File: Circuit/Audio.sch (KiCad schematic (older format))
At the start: 10 parts, among them U5 NAU8814

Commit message: Speaker choice changed & footprint creation.
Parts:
- MK1: footprint (none) -> libs1:MEMSMicrophone-SMT-SPU0410HR5H‐PB
- SP1: footprint (none) -> libs1:CVS-1508.Speaker.PCPins; Digikey PN 102-2494-ND -> 102-2498-ND; Link http://www.digikey.com.au/product-detail/en/cui-inc/CDM-120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 -> http://www.digikey.com.au/product-detail/en/cui-inc/CVS-150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; Manufacturer PN CDM-12008 -> CVS-1508; Unit Cost 2.44000 -> 3.3600
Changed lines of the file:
@@
 F 0 "SP1" H 7400 3150 50  0000 C CNN
 F 1 "SPEAKER" H 7400 2650 50  0000 C CNN
-F 2 "" H 7500 2900 50  0001 C CNN
+F 2 "libs1:CVS-1508.Speaker.PCPins" H 7500 2900 50  0001 C CNN
 F 3 "" H 7500 2900 50  0000 C CNN
-F 4 "http://www.digikey.com.au/product-detail/en/cui-inc/CDM-12008/102-2494-ND/2791824" H 7500 2900 60  0001 C CNN "Link"
-F 5 "2.44000" H 7500 2900 60  0001 C CNN "Unit Cost"
-F 6 "102-2494-ND" H 7500 2900 60  0001 C CNN "Digikey PN"
-F 7 "CDM-12008" H 7500 2900 60  0001 C CNN "Manufacturer PN"
+F 4 "http://www.digikey.com.au/product-detail/en/cui-inc/CVS-1508/102-2498-ND/2791828" H 7500 2900 60  0001 C CNN "Link"
+F 5 "3.3600" H 7500 2900 60  0001 C CNN "Unit Cost"
+F 6 "102-2498-ND" H 7500 2900 60  0001 C CNN "Digikey PN"
+F 7 "CVS-1508" H 7500 2900 60  0001 C CNN "Manufacturer PN"
 	1    7500 2900
 	1    0    0    -1
@@
 F 0 "MK1" H 1200 2200 60  0000 C CNN
 F 1 "SPU0410HR5H" H 900 1550 60  0000 C CNN
-F 2 "" H 1400 1900 60  0001 C CNN
+F 2 "libs1:MEMSMicrophone-SMT-SPU0410HR5H‐PB" H 1400 1900 60  0001 C CNN
 F 3 "" H 1400 1900 60  0001 C CNN
 	1    1400 1900

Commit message: Begin adding fields to components.
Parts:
- U5: Digikey PN (none) -> NAU8814YG-ND; Link (none) -> http://www.digikey.com.au/product-detail/en/nuvoton-technol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; Manufacturer PN (none) -> NAU8814YG; Unit Price (none) -> 3.06
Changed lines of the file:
@@
 F 2 "" H 5600 3750 60  0001 C CNN
 F 3 "" H 5600 3750 60  0001 C CNN
+F 4 "NAU8814YG-ND" H 5600 3750 60  0001 C CNN "Digikey PN"
+F 5 "http://www.digikey.com.au/product-detail/en/nuvoton-technology-corporation-of-america/NAU8814YG/NAU8814YG-ND/4271437" H 5600 3750 60  0001 C CNN "Link"
+F 6 "NAU8814YG" H 5600 3750 60  0001 C CNN "Manufacturer PN"
+F 7 "3.06" H 5600 3750 60  0001 C CNN "Unit Price"
 	1    5600 3750
 	1    0    0    -1

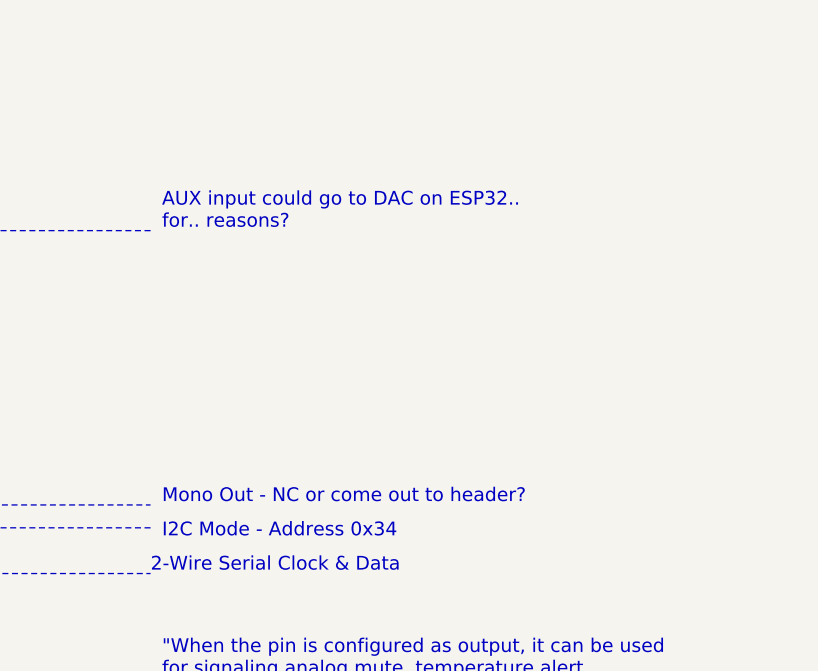
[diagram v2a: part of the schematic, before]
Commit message: IR receiver schematic & footprint.
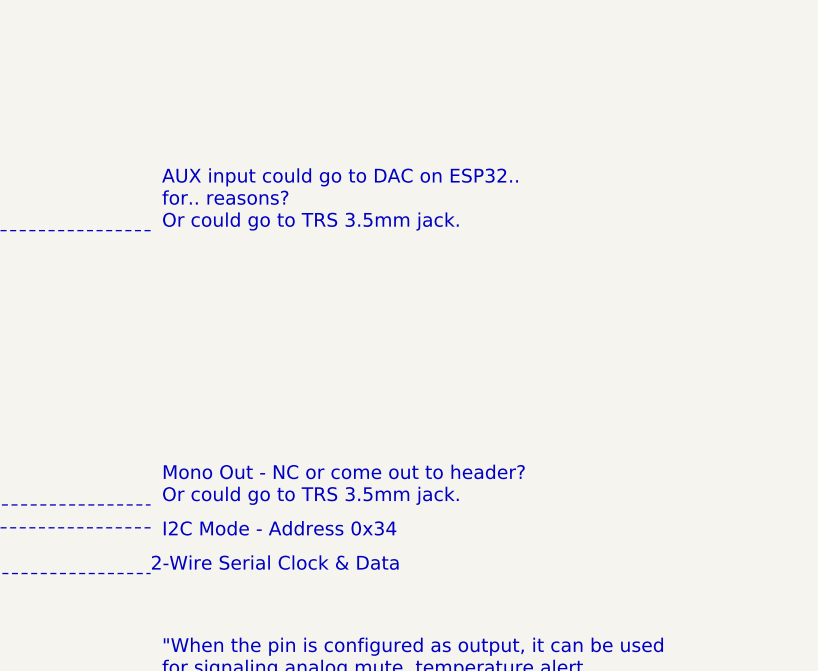
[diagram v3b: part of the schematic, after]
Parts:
- C1, C13, C14, C15, C16: footprint (none) -> Capacitors_SMD:C_0603_HandSoldering; Digikey PN (none) -> 1276-2087-1-ND; Link (none) -> http://www.digikey.com.au/product-detail/en/samsung-electro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; Manufacturer PN (none) -> CL10B475KQ8NQNC; Unit Cost (none) -> 0.01
- MK1: footprint libs1:MEMSMicrophone-SMT-SPU0410HR5H‐PB -> libs:MEMSMicrophone-SMT-SPU0410HR5H‐PB
- SP1: footprint libs1:CVS-1508.Speaker.PCPins -> libs:CVS-1508.Speaker.PCPins
- U5: footprint (none) -> libs:NAU8814_QFN-24_4x4mm_Pitch0.5mm_EPAD
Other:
- note added: "AUX input could go to DAC on ESP32..\nfor.. reasons?\nOr could go to TRS 3.5mm jack."
- note added: "Mono Out - NC or come out to header?\nOr could go to TRS 3.5mm jack."
- note removed: "AUX input could go to DAC on ESP32..\nfor.. reasons?"
- note removed: "Mono Out - NC or come out to header?"
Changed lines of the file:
@@
 F 0 "U5" H 5000 4450 60  0000 C CNN
 F 1 "NAU8814" H 6150 3050 60  0000 C CNN
-F 2 "" H 5600 3750 60  0001 C CNN
+F 2 "libs:NAU8814_QFN-24_4x4mm_Pitch0.5mm_EPAD" H 5600 3750 60  0001 C CNN
 F 3 "" H 5600 3750 60  0001 C CNN
 F 4 "NAU8814YG-ND" H 5600 3750 60  0001 C CNN "Digikey PN"
@@
 F 0 "SP1" H 7400 3150 50  0000 C CNN
 F 1 "SPEAKER" H 7400 2650 50  0000 C CNN
-F 2 "libs1:CVS-1508.Speaker.PCPins" H 7500 2900 50  0001 C CNN
+F 2 "libs:CVS-1508.Speaker.PCPins" H 7500 2900 50  0001 C CNN
 F 3 "" H 7500 2900 50  0000 C CNN
 F 4 "http://www.digikey.com.au/product-detail/en/cui-inc/CVS-1508/102-2498-ND/2791828" H 7500 2900 60  0001 C CNN "Link"
@@
 F 0 "MK1" H 1200 2200 60  0000 C CNN
 F 1 "SPU0410HR5H" H 900 1550 60  0000 C CNN
-F 2 "libs1:MEMSMicrophone-SMT-SPU0410HR5H‐PB" H 1400 1900 60  0001 C CNN
+F 2 "libs:MEMSMicrophone-SMT-SPU0410HR5H‐PB" H 1400 1900 60  0001 C CNN
 F 3 "" H 1400 1900 60  0001 C CNN
 	1    1400 1900
@@
 F 0 "C16" H 5575 2400 50  0000 L CNN
 F 1 "4.7uF" H 5575 2200 50  0000 L CNN
-F 2 "" H 5588 2150 50  0001 C CNN
+F 2 "Capacitors_SMD:C_0603_HandSoldering" H 5588 2150 50  0001 C CNN
 F 3 "" H 5550 2300 50  0000 C CNN
+F 4 "1276-2087-1-ND" H 3600 4150 60  0001 C CNN "Digikey PN"
+F 5 "http://www.digikey.com.au/product-detail/en/samsung-electro-mechanics-america-inc/CL10B475KQ8NQNC/1276-2087-1-ND/3890173" H 3600 4150 60  0001 C CNN "Link"
+F 6 "CL10B475KQ8NQNC" H 3600 4150 60  0001 C CNN "Manufacturer PN"
+F 7 "0.01" H 3600 4150 60  0001 C CNN "Unit Cost"
 	1    5550 2300
 	1    0    0    -1
@@
 F 0 "C13" H 3625 4250 50  0000 L CNN
 F 1 "4.7uF" H 3625 4050 50  0000 L CNN
-F 2 "" H 3638 4000 50  0001 C CNN
+F 2 "Capacitors_SMD:C_0603_HandSoldering" H 3638 4000 50  0001 C CNN
 F 3 "" H 3600 4150 50  0000 C CNN
+F 4 "1276-2087-1-ND" H 3600 4150 60  0001 C CNN "Digikey PN"
+F 5 "http://www.digikey.com.au/product-detail/en/samsung-electro-mechanics-america-inc/CL10B475KQ8NQNC/1276-2087-1-ND/3890173" H 3600 4150 60  0001 C CNN "Link"
+F 6 "CL10B475KQ8NQNC" H 3600 4150 60  0001 C CNN "Manufacturer PN"
+F 7 "0.01" H 3600 4150 60  0001 C CNN "Unit Cost"
 	1    3600 4150
 	1    0    0    -1
@@
 F 0 "C14" H 3875 4250 50  0000 L CNN
 F 1 "4.7uF" H 3875 4050 50  0000 L CNN
-F 2 "" H 3888 4000 50  0001 C CNN
+F 2 "Capacitors_SMD:C_0603_HandSoldering" H 3888 4000 50  0001 C CNN
 F 3 "" H 3850 4150 50  0000 C CNN
+F 4 "1276-2087-1-ND" H 3600 4150 60  0001 C CNN "Digikey PN"
+F 5 "http://www.digikey.com.au/product-detail/en/samsung-electro-mechanics-america-inc/CL10B475KQ8NQNC/1276-2087-1-ND/3890173" H 3600 4150 60  0001 C CNN "Link"
+F 6 "CL10B475KQ8NQNC" H 3600 4150 60  0001 C CNN "Manufacturer PN"
+F 7 "0.01" H 3600 4150 60  0001 C CNN "Unit Cost"
 	1    3850 4150
 	1    0    0    -1
@@
 F 0 "C15" H 4125 4250 50  0000 L CNN
 F 1 "4.7uF" H 4125 4050 50  0000 L CNN
-F 2 "" H 4138 4000 50  0001 C CNN
+F 2 "Capacitors_SMD:C_0603_HandSoldering" H 4138 4000 50  0001 C CNN
 F 3 "" H 4100 4150 50  0000 C CNN
+F 4 "1276-2087-1-ND" H 3600 4150 60  0001 C CNN "Digikey PN"
+F 5 "http://www.digikey.com.au/product-detail/en/samsung-electro-mechanics-america-inc/CL10B475KQ8NQNC/1276-2087-1-ND/3890173" H 3600 4150 60  0001 C CNN "Link"
+F 6 "CL10B475KQ8NQNC" H 3600 4150 60  0001 C CNN "Manufacturer PN"
+F 7 "0.01" H 3600 4150 60  0001 C CNN "Unit Cost"
 	1    4100 4150
 	1    0    0    -1
@@
 F 0 "C1" H 825 2000 50  0000 L CNN
 F 1 "4.7uF" H 825 1800 50  0000 L CNN
-F 2 "" H 838 1750 50  0001 C CNN
+F 2 "Capacitors_SMD:C_0603_HandSoldering" H 838 1750 50  0001 C CNN
 F 3 "" H 800 1900 50  0000 C CNN
+F 4 "1276-2087-1-ND" H 3600 4150 60  0001 C CNN "Digikey PN"
+F 5 "http://www.digikey.com.au/product-detail/en/samsung-electro-mechanics-america-inc/CL10B475KQ8NQNC/1276-2087-1-ND/3890173" H 3600 4150 60  0001 C CNN "Link"
+F 6 "CL10B475KQ8NQNC" H 3600 4150 60  0001 C CNN "Manufacturer PN"
+F 7 "0.01" H 3600 4150 60  0001 C CNN "Unit Cost"
 	1    800  1900
 	1    0    0    -1
@@
 	6800 3700 9550 3700
 Text Notes 9600 3700 0    60   ~ 0
-Mono Out - NC or come out to header?
+Mono Out - NC or come out to header?\nOr could go to TRS 3.5mm jack.
 $Comp
 L GND #PWR063
@@
 	5650 2500 5650 2800
 Text Notes 9600 2500 0    60   ~ 0
-AUX input could go to DAC on ESP32..\nfor.. reasons?
+AUX input could go to DAC on ESP32..\nfor.. reasons?\nOr could go to TRS 3.5mm jack.
 $Comp
 L GND #PWR066

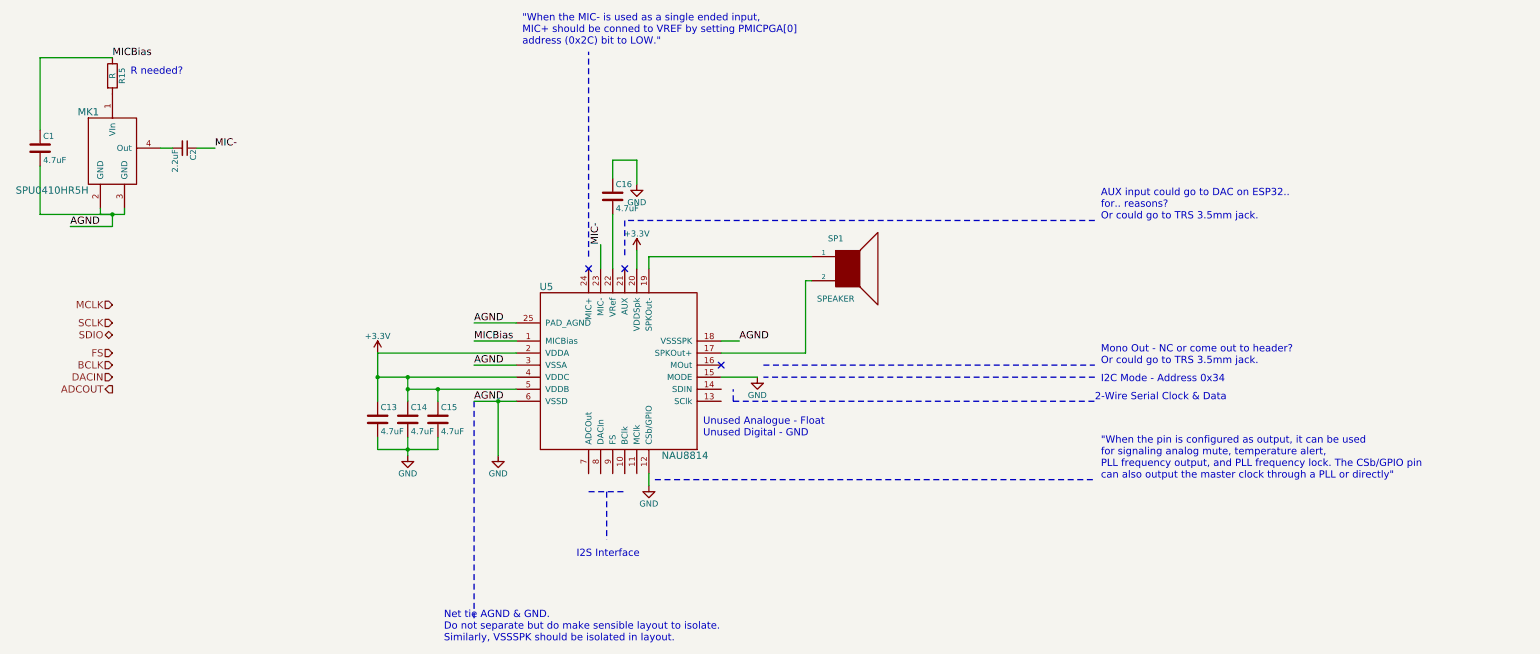
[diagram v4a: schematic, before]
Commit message: Adding some component information, connecting audio.
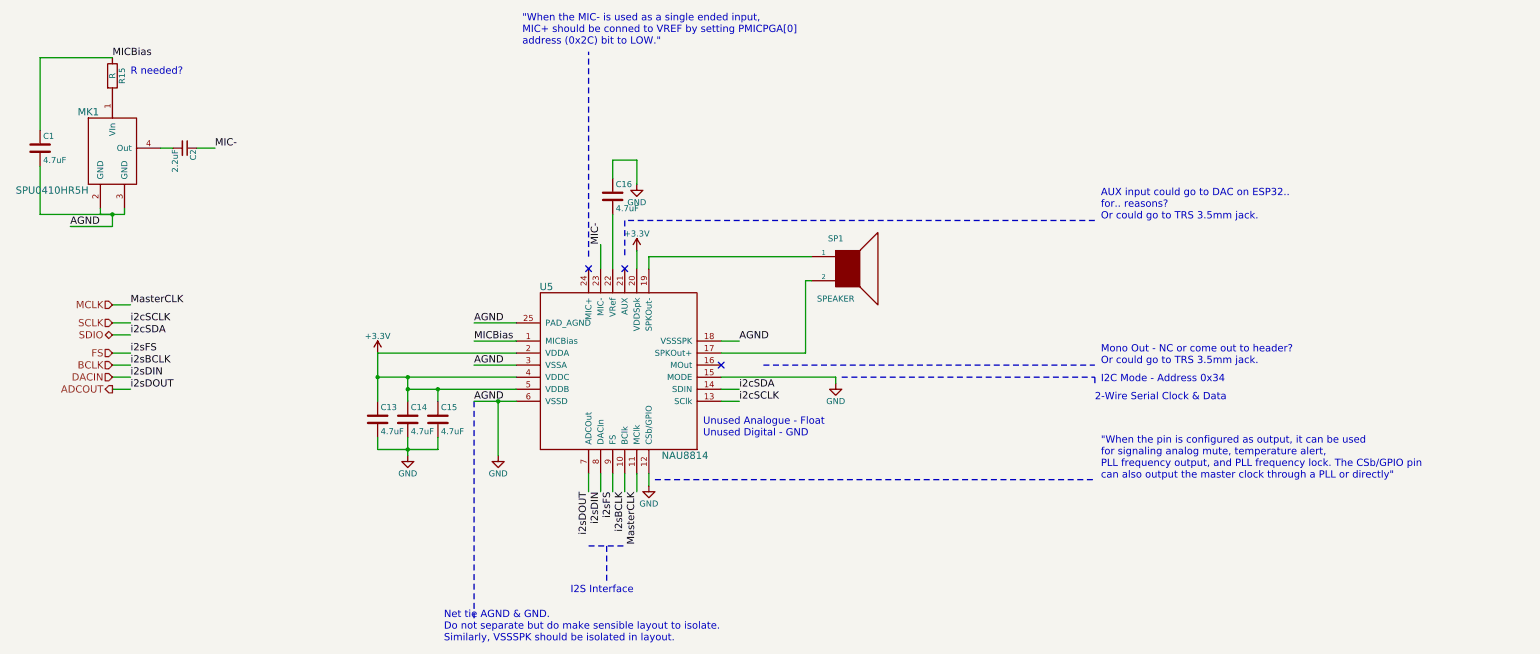
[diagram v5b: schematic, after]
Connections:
- net ADCOUT: now also U5.7 (ADCOut)
- net BCLK: now also U5.10 (BClk)
- net DACIN: now also U5.8 (DACIn)
- net FS: now also U5.9 (FS)
- net MCLK: now also U5.11 (MClk)
- net SCLK: now also U5.13 (SClk)
- net SDIO: now also U5.14 (SDIN)
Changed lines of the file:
@@
 L GND #PWR061
 U 1 1 581BF41C
-P 6750 3800
-F 0 "#PWR061" H 6750 3550 50  0001 C CNN
-F 1 "GND" H 6750 3650 50  0000 C CNN
-F 2 "" H 6750 3800 50  0000 C CNN
-F 3 "" H 6750 3800 50  0000 C CNN
-	1    6750 3800
-	1    0    0    -1
-$EndComp
-Wire Wire Line
-	6450 3800 6750 3800
+P 7400 3850
+F 0 "#PWR061" H 7400 3600 50  0001 C CNN
+F 1 "GND" H 7400 3700 50  0000 C CNN
+F 2 "" H 7400 3850 50  0000 C CNN
+F 3 "" H 7400 3850 50  0000 C CNN
+	1    7400 3850
+	1    0    0    -1
+$EndComp
+Wire Wire Line
+	6450 3800 7400 3800
 Text Notes 9600 3850 0    60   ~ 0
 I2C Mode - Address 0x34
@@
 Wire Wire Line
 	7150 3600 6450 3600
-Wire Notes Line
-	9550 3800 6800 3800
 Wire Notes Line
 	6800 3700 9550 3700
@@
 "When the pin is configured as output, it can be used\nfor signaling analog mute, temperature alert, \nPLL frequency output, and PLL frequency lock. The CSb/GPIO pin\ncan also output the master clock through a PLL or directly"
 NoConn ~ 6450 3700
-Wire Notes Line
-	6550 4000 9550 4000
 Text Notes 9550 4000 0    60   ~ 0
  2-Wire Serial Clock & Data
 Wire Notes Line
-	6550 4000 6550 3900
-Wire Notes Line
-	5350 4750 5650 4750
-Wire Notes Line
-	5500 4750 5500 5150
-Text Notes 5250 5300 0    60   ~ 0
-I2S Interface
+	5350 5200 5650 5200
 Text HLabel 1400 3200 0    60   Input ~ 0
 MCLK
@@
 Text HLabel 1400 3900 0    60   Output ~ 0
 ADCOUT
+Text Label 1550 3350 0    60   ~ 0
+i2cSCLK
+Text Label 1550 3450 0    60   ~ 0
+i2cSDA
+Text Label 1550 3600 0    60   ~ 0
+i2sFS
+Text Label 1550 3700 0    60   ~ 0
+i2sBCLK
+Text Label 1550 3800 0    60   ~ 0
+i2sDIN
+Text Label 1550 3900 0    60   ~ 0
+i2sDOUT
+Text Label 1550 3200 0    60   ~ 0
+MasterCLK
+Text Label 5750 4750 3    60   ~ 0
+MasterCLK
+Text Label 5550 4750 3    60   ~ 0
+i2sFS
+Text Label 5650 4750 3    60   ~ 0
+i2sBCLK
+Text Label 5450 4750 3    60   ~ 0
+i2sDIN
+Text Label 5350 4750 3    60   ~ 0
+i2sDOUT
+Text Notes 5200 5600 0    60   ~ 0
+I2S Interface
+Wire Notes Line
+	5500 5200 5500 5500
+Wire Wire Line
+	5350 4600 5350 4750
+Wire Wire Line
+	5450 4600 5450 4750
+Wire Wire Line
+	5550 4600 5550 4750
+Wire Wire Line
+	5650 4600 5650 4750
+Wire Wire Line
+	5750 4600 5750 4750
+Text Label 6600 4000 0    60   ~ 0
+i2cSCLK
+Text Label 6600 3900 0    60   ~ 0
+i2cSDA
+Wire Wire Line
+	7400 3800 7400 3850
+Wire Notes Line
+	7450 3800 9550 3800
+Wire Notes Line
+	9550 3800 9550 3850
+Wire Wire Line
+	6450 3900 6600 3900
+Wire Wire Line
+	6450 4000 6600 4000
+Wire Wire Line
+	1400 3200 1550 3200
+Wire Wire Line
+	1400 3350 1550 3350
+Wire Wire Line
+	1400 3450 1550 3450
+Wire Wire Line
+	1400 3600 1550 3600
+Wire Wire Line
+	1400 3700 1550 3700
+Wire Wire Line
+	1400 3800 1550 3800
+Wire Wire Line
+	1400 3900 1550 3900
 $EndSCHEMATC

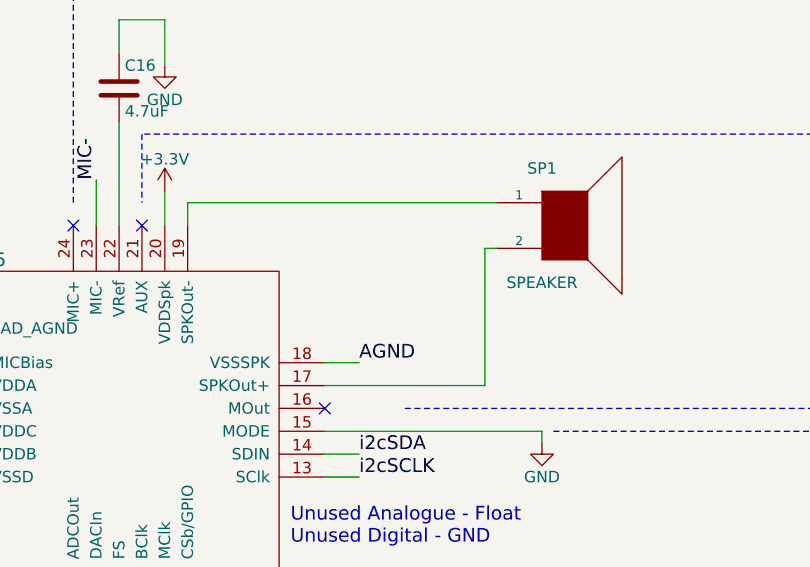
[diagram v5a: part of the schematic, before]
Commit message: Some small caps on the speaker output to balance and filter.
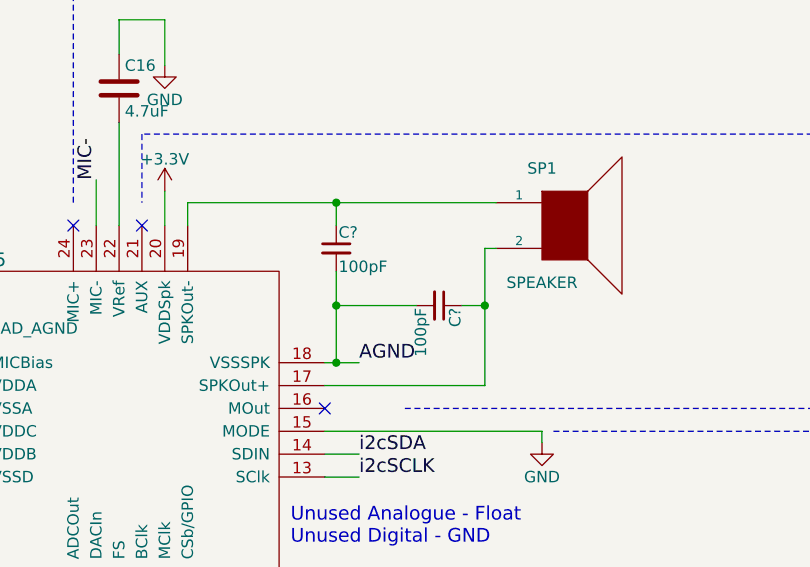
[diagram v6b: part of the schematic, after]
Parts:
- added C? (x2): 100pF, symbol C_Small
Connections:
- net GND: now also C?.2, C?.2
- net at SP1.2, U5.17 (SPKOut+): now also C?.1
- net at SP1.1, U5.19 (SPKOut-): now also C?.1
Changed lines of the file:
@@
 Wire Wire Line
 	1400 3900 1550 3900
+$Comp
+L C_Small C?
+U 1 1 581FF4BD
+P 6950 3250
+F 0 "C?" H 6960 3320 50  0000 L CNN
+F 1 "100pF" H 6960 3170 50  0000 L CNN
+F 2 "" H 6950 3250 50  0000 C CNN
+F 3 "" H 6950 3250 50  0000 C CNN
+F 4 "490-3160-1-ND" H 6950 3250 60  0001 C CNN "Digikey PN"
+F 5 "http://www.digikey.com.au/product-detail/en/murata-electronics-north-america/GRM0335C1E101JA01D/490-3160-1-ND/702701" H 6950 3250 60  0001 C CNN "Link"
+F 6 "GRM0335C1E101JA01D" H 6950 3250 60  0001 C CNN "Manufacturer PN"
+F 7 "0.01" H 6950 3250 60  0001 C CNN "Unit Cost"
+	1    6950 3250
+	0    1    1    0
+$EndComp
+$Comp
+L C_Small C?
+U 1 1 5820032A
+P 6500 3000
+F 0 "C?" H 6510 3070 50  0000 L CNN
+F 1 "100pF" H 6510 2920 50  0000 L CNN
+F 2 "" H 6500 3000 50  0000 C CNN
+F 3 "" H 6500 3000 50  0000 C CNN
+F 4 "490-3160-1-ND" H 6500 3000 60  0001 C CNN "Digikey PN"
+F 5 "http://www.digikey.com.au/product-detail/en/murata-electronics-north-america/GRM0335C1E101JA01D/490-3160-1-ND/702701" H 6500 3000 60  0001 C CNN "Link"
+F 6 "GRM0335C1E101JA01D" H 6500 3000 60  0001 C CNN "Manufacturer PN"
+F 7 "0.01" H 6500 3000 60  0001 C CNN "Unit Cost"
+	1    6500 3000
+	1    0    0    -1
+$EndComp
+Wire Wire Line
+	6500 2800 6500 2900
+Connection ~ 6500 2800
+Wire Wire Line
+	7150 3250 7050 3250
+Connection ~ 7150 3250
+Wire Wire Line
+	6850 3250 6500 3250
+Wire Wire Line
+	6500 3100 6500 3500
+Connection ~ 6500 3500
+Connection ~ 6500 3250
 $EndSCHEMATC

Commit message: Audio components BOM data.
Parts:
- C2: Digikey PN (none) -> 490-3296-1-ND; Link (none) -> http://www.digikey.com.au/product-detail/en/murata-electron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; Manufacturer PN (none) -> GRM188R61C225KE15D; Unit Cost (none) -> 0.12
- C? (x2): footprint (none) -> Capacitors_SMD:C_0603_HandSoldering
- MK1: Digikey PN (none) -> 423-1138-1-ND; Link (none) -> http://www.digikey.com.au/product-detail/en/knowles/SPU0410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; Manufacturer PN (none) -> SPU0410HR5H-PB; Unit Cost (none) -> 0.92000
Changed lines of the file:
@@
 F 2 "libs:MEMSMicrophone-SMT-SPU0410HR5H‐PB" H 1400 1900 60  0001 C CNN
 F 3 "" H 1400 1900 60  0001 C CNN
+F 4 "423-1138-1-ND" H 1400 1900 60  0001 C CNN "Digikey PN"
+F 5 "http://www.digikey.com.au/product-detail/en/knowles/SPU0410HR5H-PB/423-1138-1-ND/2420982" H 1400 1900 60  0001 C CNN "Link"
+F 6 "SPU0410HR5H-PB" H 1400 1900 60  0001 C CNN "Manufacturer PN"
+F 7 "0.92000" H 1400 1900 60  0001 C CNN "Unit Cost"
 	1    1400 1900
 	1    0    0    -1
@@
 F 2 "" H 2000 1900 50  0001 C CNN
 F 3 "" H 2000 1900 50  0000 C CNN
+F 4 "490-3296-1-ND" H 2000 1900 60  0001 C CNN "Digikey PN"
+F 5 "http://www.digikey.com.au/product-detail/en/murata-electronics-north-america/GRM188R61C225KE15D/490-3296-1-ND/702837" H 2000 1900 60  0001 C CNN "Link"
+F 6 "GRM188R61C225KE15D" H 2000 1900 60  0001 C CNN "Manufacturer PN"
+F 7 "0.12" H 2000 1900 60  0001 C CNN "Unit Cost"
 	1    2000 1900
 	0    1    1    0
@@
 F 0 "C?" H 6960 3320 50  0000 L CNN
 F 1 "100pF" H 6960 3170 50  0000 L CNN
-F 2 "" H 6950 3250 50  0000 C CNN
+F 2 "Capacitors_SMD:C_0603_HandSoldering" H 6950 3250 50  0001 C CNN
 F 3 "" H 6950 3250 50  0000 C CNN
 F 4 "490-3160-1-ND" H 6950 3250 60  0001 C CNN "Digikey PN"
@@
 F 0 "C?" H 6510 3070 50  0000 L CNN
 F 1 "100pF" H 6510 2920 50  0000 L CNN
-F 2 "" H 6500 3000 50  0000 C CNN
+F 2 "Capacitors_SMD:C_0603_HandSoldering" H 6500 3000 50  0001 C CNN
 F 3 "" H 6500 3000 50  0000 C CNN
 F 4 "490-3160-1-ND" H 6500 3000 60  0001 C CNN "Digikey PN"
